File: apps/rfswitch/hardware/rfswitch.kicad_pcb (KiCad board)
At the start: 2 copper layers, 94.9 x 96 mm, 56 parts, among them J1 CONN_AC, J10 CONN_O4, J2 CONN_O1, J3 CONN_AC_SW1, J4 CONN_AC_SW2, J5 CONN_01X05, J6 CONN_O2, J7 CONN_AC_SW3, J8 CONN_O3, J9 CONN_AC_SW4, Q1 Q_NPN_BEC, Q2 Q_NPN_BEC, Q3 Q_NPN_BEC, Q4 Q_NPN_BEC, U1 HLK-PM01, U10 G3MB-202P-5V, U2 SFH6916, U3 G3MB-202P-5V, U5 G3MB-202P-5V, U6 TINY328, U8 G3MB-202P-5V

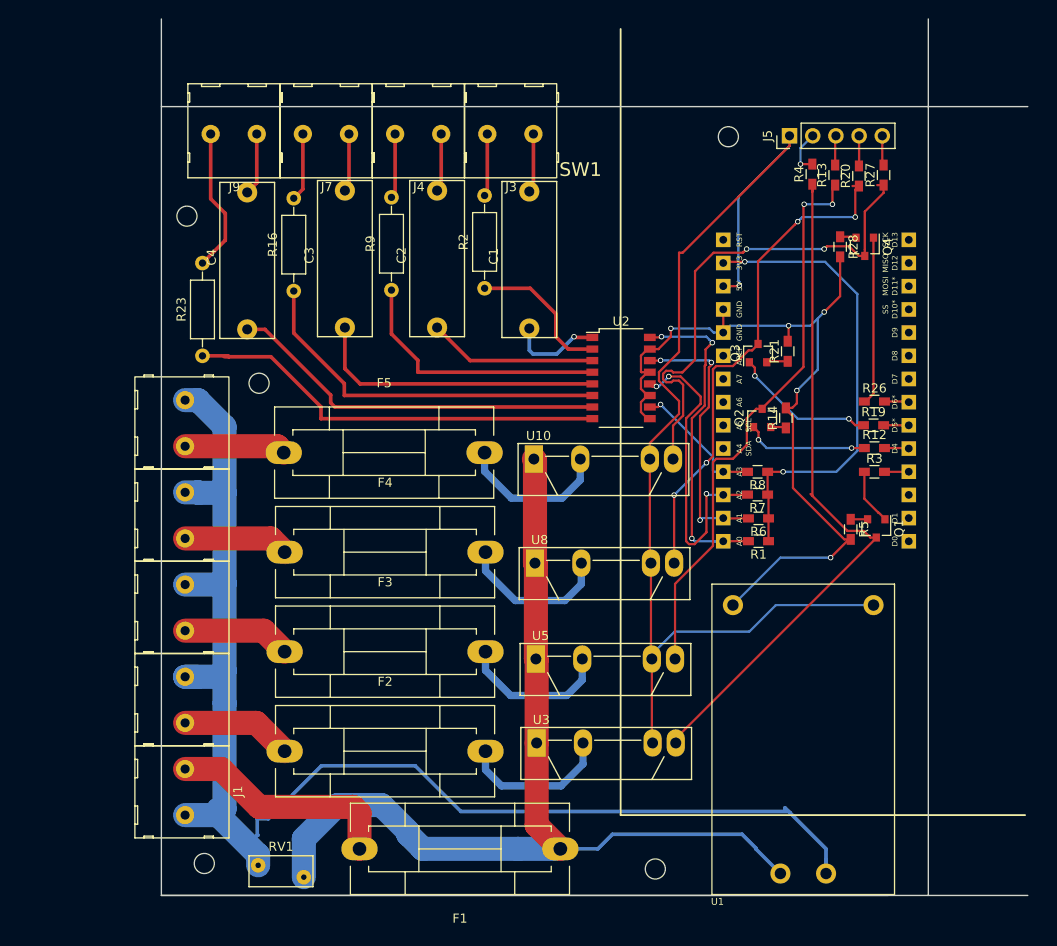
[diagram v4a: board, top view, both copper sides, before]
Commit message: Fix pulldown resistor on transistors that wasn't in the right position
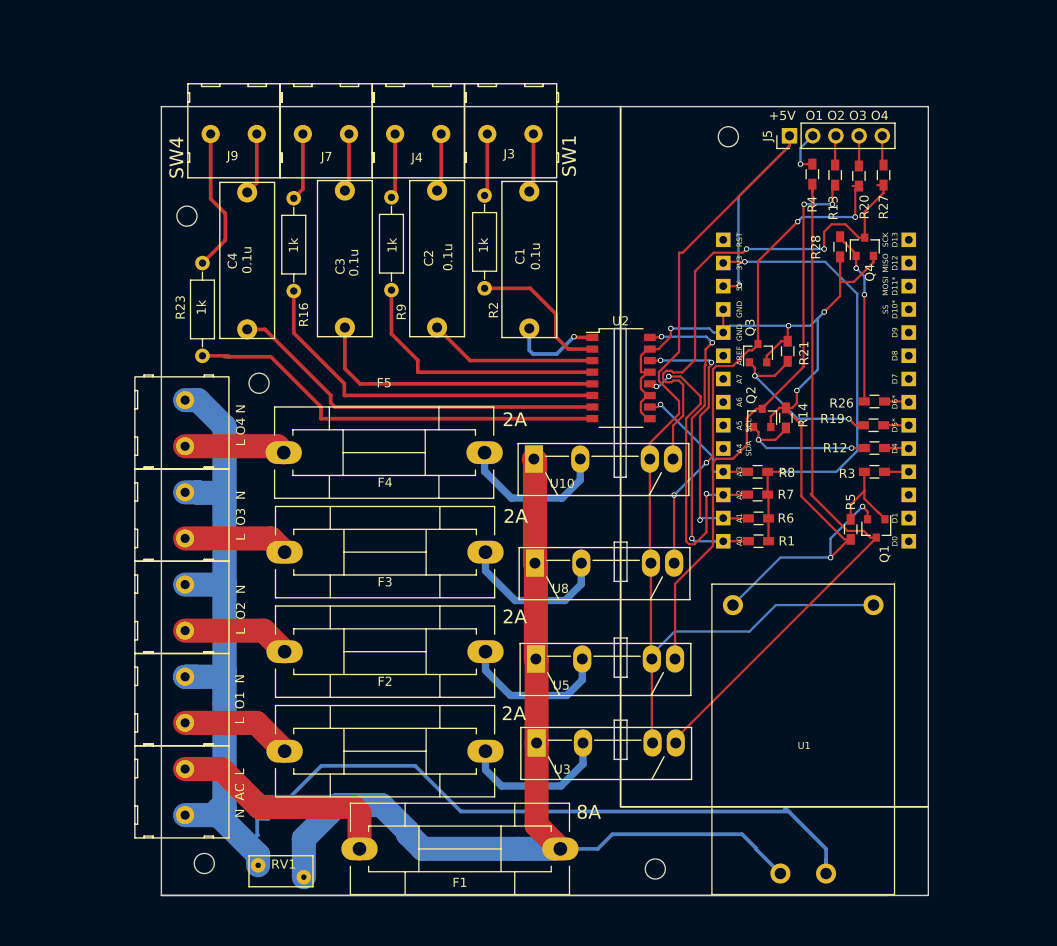
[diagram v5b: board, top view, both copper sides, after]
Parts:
- R12, R19, R26, R3: value 330 -> 10k
- turned Q4 to 90 degrees
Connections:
- Q1 pad 2: Net-(Q1-Pad2) -> GND
- Q2 pad 2: Net-(Q2-Pad2) -> GND
- Q3 pad 2: Net-(Q3-Pad2) -> GND
- Q4 pad 2: Net-(Q4-Pad2) -> GND
- R14 pad 1: Net-(Q2-Pad2) -> Net-(Q2-Pad1)
- R21 pad 1: Net-(Q3-Pad2) -> Net-(Q3-Pad1)
- R28 pad 1: Net-(Q4-Pad2) -> Net-(Q4-Pad1)
- R5 pad 1: Net-(Q1-Pad2) -> Net-(Q1-Pad1)
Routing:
- net GND: track 89.1 -> 110.1 mm, vias 5 -> 6
- net Net-(Q3-Pad1): track 15.9 -> 20.2 mm
- net Net-(Q2-Pad1): track 13.6 -> 17.4 mm
- net Net-(Q1-Pad1): track 6.16 -> 9.88 mm
- net Net-(Q3-Pad2): track 2.34 -> 0.00 mm
- net Net-(Q1-Pad2): track 1.85 -> 0.00 mm
- net Net-(Q4-Pad2): track 1.79 -> 0.00 mm
- net Net-(Q2-Pad2): track 1.69 -> 0.00 mm
- net Net-(Q4-Pad1): track 18.4 -> 19.3 mm, vias 0 -> 2
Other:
- board size 94.9 x 96 mm -> 84 x 86.4 mm
- board text added: "+5V"
- board text added: "2A"
- board text added: "8A"
- board text added: "L O1 N"
- board text added: "L O2 N"
- board text added: "L O3 N"
- board text added: "L O4 N"
- board text added: "N AC L"
- board text added: "O1 O2 O3 O4"
- board text added: "SW4"

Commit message: Various fixes after first order
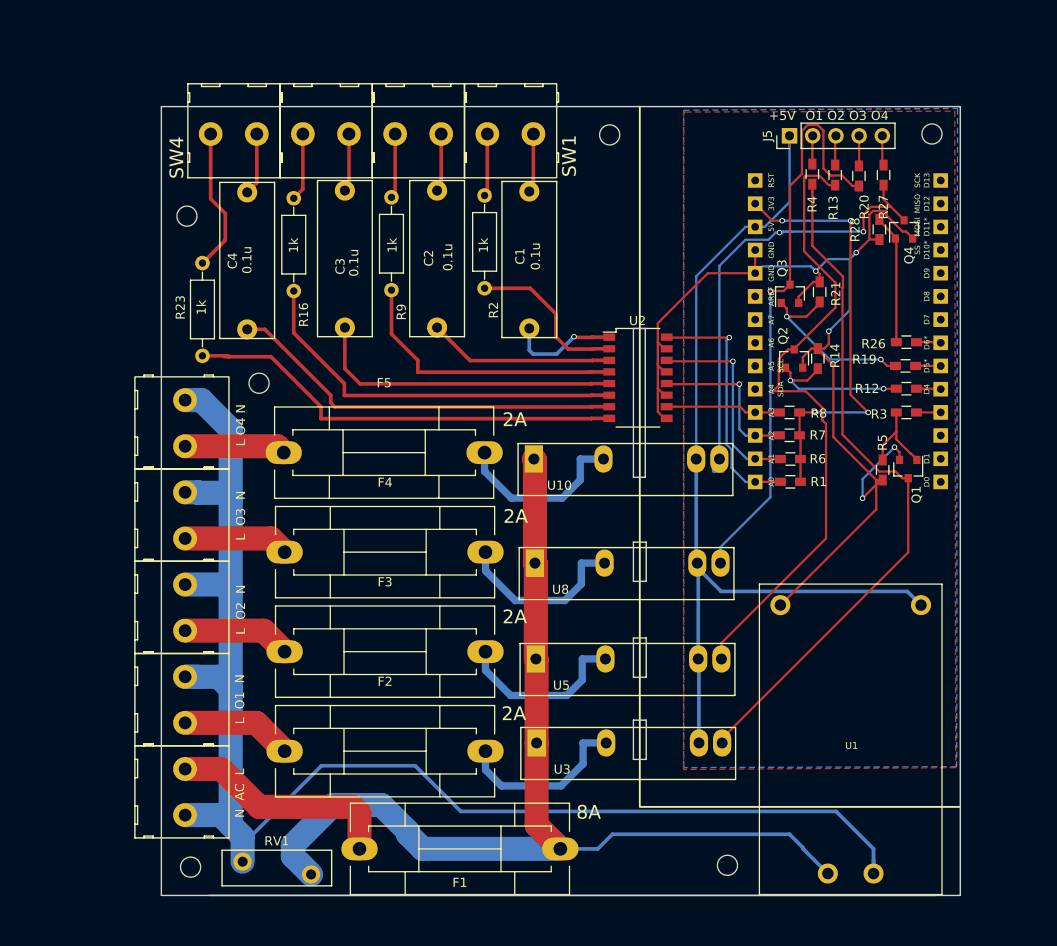
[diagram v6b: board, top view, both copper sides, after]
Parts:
- added REF**: MountingHole_2.2mm_M2, Mounting_Holes:MountingHole_2.2mm_M2, F.Cu at (137.1, 35.5)
- RV1: footprint Varistors:RV_Disc_D7_W3.4_P5 -> Varistors:RV_Disc_D12_W3.9_P7.5
- U10, U3, U5, U8: footprint Housings_SIP:SIP4_Sharp-SSR_Pitch7.62mm_Straight -> mylib:G3MB-202P-5V
- moved REF** 22.3 mm to (172.4, 35.4)
- moved REF** 7.91 mm to (150.0, 115.5)
- moved Q1 7.38 mm to (169.8, 72.1)
- moved Q2 7.38 mm to (157.3, 60.0)
- moved Q3 7.38 mm to (156.8, 52.9)
- moved R1 7.38 mm to (156.9, 73.5)
- moved R12 7.38 mm to (169.6, 63.3)
- moved R14 7.38 mm to (159.9, 60.0)
- moved R19 7.38 mm to (169.5, 60.8)
- moved R21 7.38 mm to (160.1, 52.7)
- moved R26 7.38 mm to (169.6, 58.2)
- moved R3 7.38 mm to (169.6, 65.9)
- moved R5 7.38 mm to (167.0, 72.2)
- moved R6 7.38 mm to (156.9, 71.0)
- moved R7 7.38 mm to (156.8, 68.4)
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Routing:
- net +5V: track 122.6 -> 99.9 mm, vias 1 -> 0
- net /SW3: track 35.2 -> 17.6 mm, vias 3 -> 1
- net GND: track 110.1 -> 121.9 mm, vias 6 -> 5
- net /SW1: track 36.9 -> 27.5 mm, vias 3 -> 1
- net Net-(Q3-Pad3): track 55.1 -> 64.2 mm, vias 4 -> 1
- net Net-(Q2-Pad3): track 62.4 -> 70.9 mm, vias 2 -> 0
- net /SW2: track 30.0 -> 22.3 mm, vias 3 -> 1
- net /LINE: track 106.5 -> 113.0 mm
- net Net-(Q4-Pad1): track 19.3 -> 14.7 mm, vias 2 -> 0
- net +3V3: track 51.8 -> 48.2 mm, vias 2 -> 4
- net Net-(Q4-Pad3): track 55.5 -> 52.8 mm
- net Net-(F5-Pad2): track 16.9 -> 19.4 mm
- net Net-(F4-Pad2): track 16.9 -> 19.5 mm
- net Net-(F3-Pad2): track 18.4 -> 21.0 mm
- net Net-(F2-Pad2): track 18.6 -> 21.2 mm
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- added copper zone on B.Cu, net +5V
- added copper zone on F.Cu, net GND
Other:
- board size 84 x 86.4 mm -> 87.5 x 86.4 mm

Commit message: Final board tweaks for construction, and first release of software
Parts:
- added BTN: CONN_BTNS, Pin_Headers:Pin_Header_Straight_1x05_Pitch2.54mm, F.Cu at (144.1, 35.6)
- LED: renamed from J5; value CONN_01X05 -> CONN_LEDS
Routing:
- net /SW4: track 12.6 -> 46.8 mm, vias 0 -> 2
- net /SW3: track 17.6 -> 45.6 mm, vias 1 -> 2
- net /SW2: track 22.3 -> 48.3 mm, vias 1 -> 2
- net /SW1: track 27.5 -> 50.8 mm, vias 1 -> 3
- net GND: track 121.9 -> 141.1 mm
- net +5V: track 99.9 -> 103.4 mm
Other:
- board text added: "1"
- board text added: "10k"
- board text added: "2"
- board text added: "2k9"
- board text added: "3"
- board text added: "330"
- board text added: "4"
- board text added: "GND"
